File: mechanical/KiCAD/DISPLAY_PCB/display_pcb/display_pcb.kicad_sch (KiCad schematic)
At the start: 52 parts, among them J1 USB_C_Receptacle_USB2.0_16P, J2 Conn_01x18_Socket, J3 Conn_01x01_Pin, J4 Conn_01x01_Pin, J5 Conn_01x02_Pin, Q1 AO3401A, Q2 FS8205, U1 ESP32-S3-WROOM-1, U2 DW01A, U3 USBLC6-2P6, U4 TP4056-42-ESOP8, U5 TLV75733PDBV

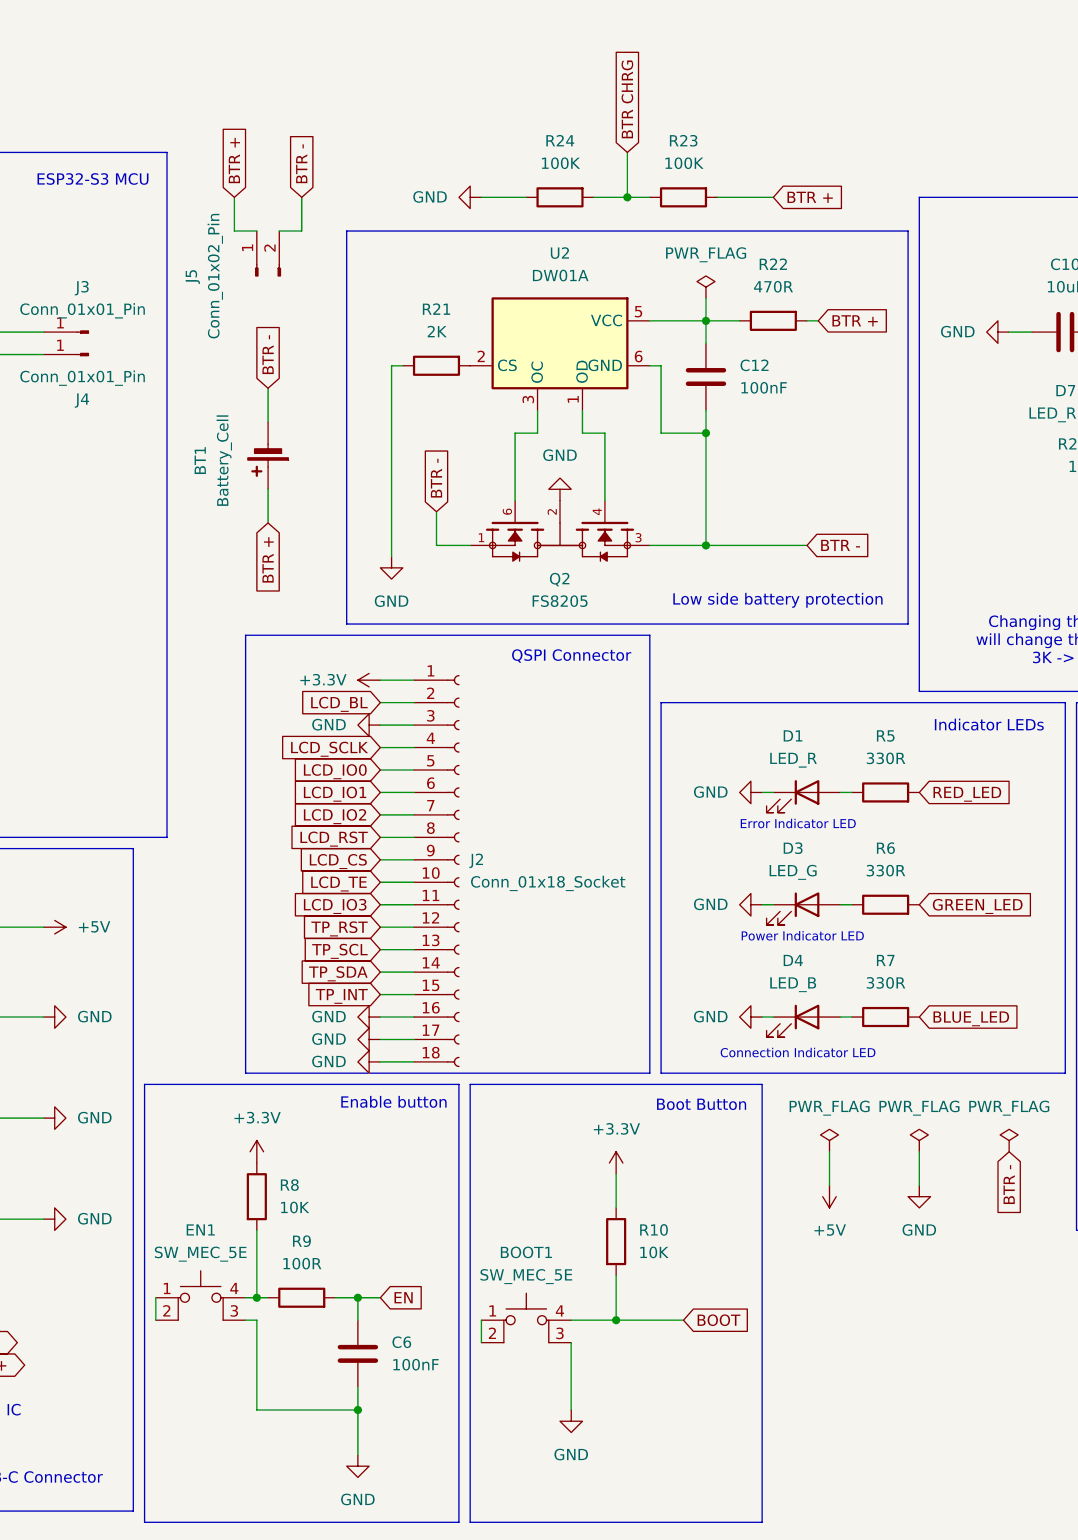
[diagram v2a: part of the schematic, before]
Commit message: Related components are grouped together, they are roughly placed on the PCB. The battery protection may have to go due space limitations (most LiPO batteries has built-in protection). The PCB will be spaced out with extra spacers so the current keepout zones on the front copper face may be used.
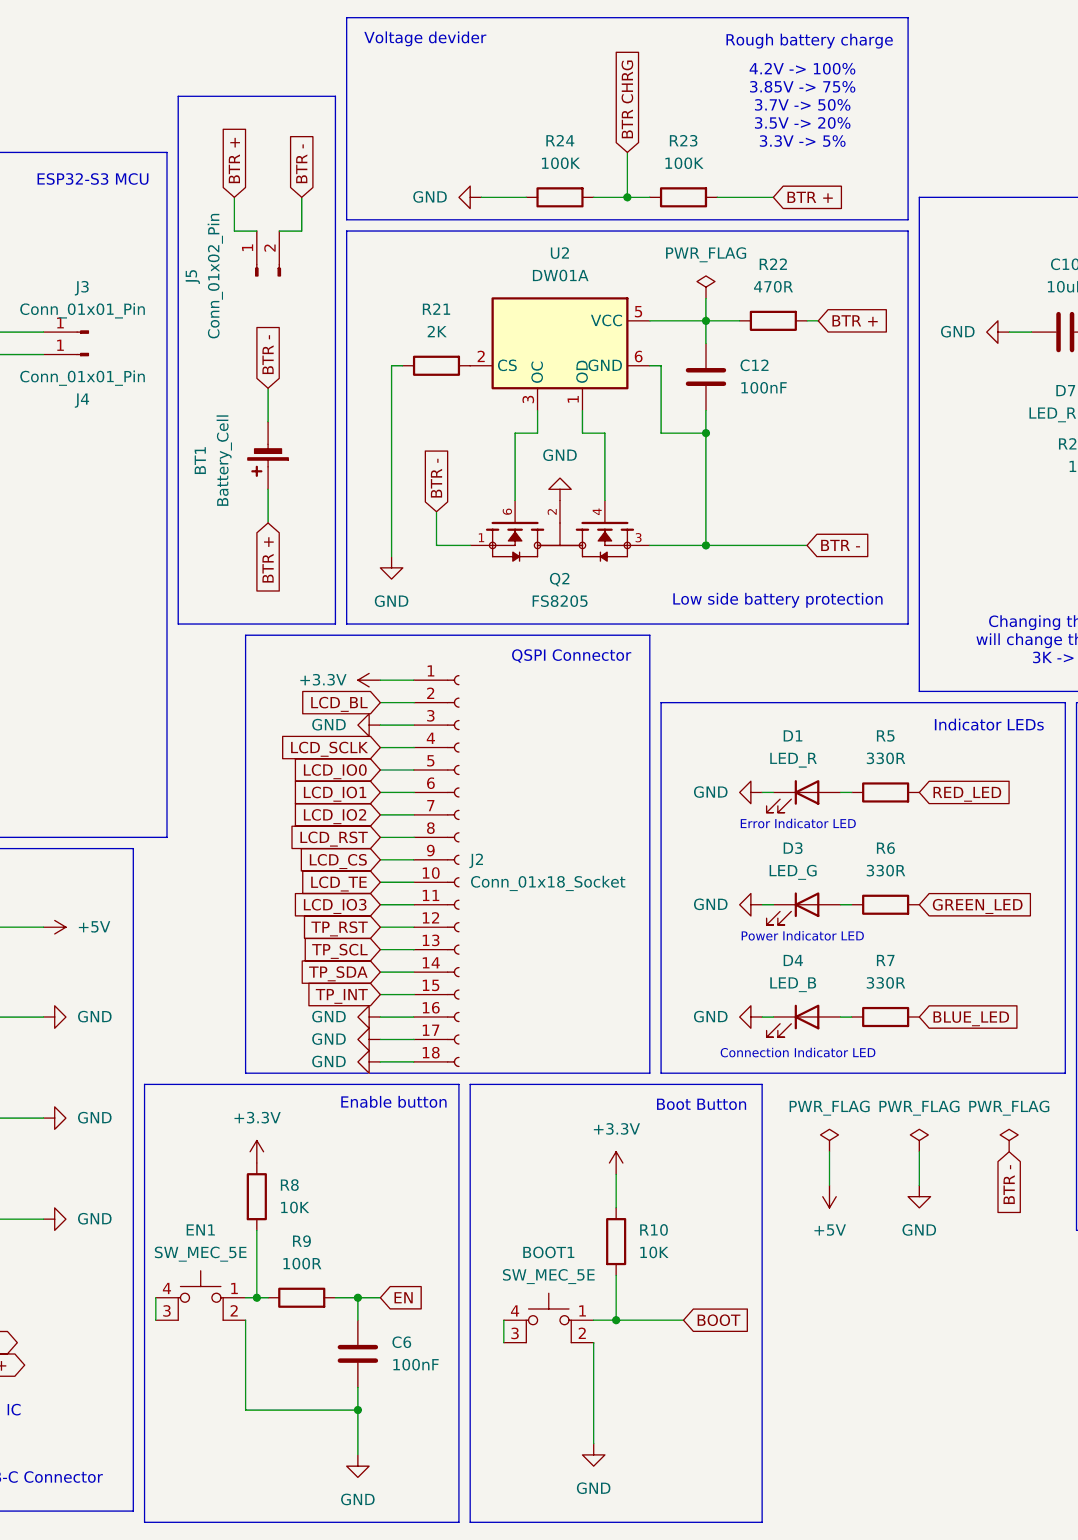
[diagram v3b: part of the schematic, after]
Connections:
- net BOOT: now also BOOT1.1; no longer BOOT1.4 (A)
- net GND: now also BOOT1.2, EN1.2; no longer BOOT1.3 (K), EN1.3 (K)
- net at R8.2, R9.1: now also EN1.1; no longer EN1.4 (A)
- new net: EN1.3 (K), EN1.4 (A)
- new net: BOOT1.3 (K), BOOT1.4 (A)
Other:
- note added: "4.2V -> 100% 3.85V -> 75% 3.7V -> 50% 3.5V -> 20% 3.3V -> 5%"
- note added: "Rough battery charge"
- note added: "Voltage devider"
- moved on the sheet: BOOT1
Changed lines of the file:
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@@
 	)
 	(rectangle
+		(start 129.54 26.67)
+		(end 193.04 49.53)
+		(stroke
+			(width 0)
+			(type default)
+		)
+		(fill
+			(type none)
+		)
+	)
+	(rectangle
 		(start 15.24 41.91)
 		(end 109.22 119.38)
@@
 	)
 	(rectangle
+		(start 110.49 35.56)
+		(end 128.27 95.25)
+		(stroke
+			(width 0)
+			(type default)
+		)
+		(fill
+			(type none)
+		)
+	)
+	(rectangle
 		(start 118.11 96.52)
 		(end 163.83 146.05)
@@
 		)
 	)
+	(text "4.2V -> 100%\n3.85V -> 75%\n3.7V -> 50%\n3.5V -> 20%\n3.3V -> 5%"
+		(exclude_from_sim no)
+		(at 181.102 36.83 0)
+		(effects
+			(font
+				(size 1.27 1.27)
+			)
+		)
+	)
 	(text "Connection Indicator LED"
 		(exclude_from_sim no)
@@
 		)
 	)
+	(text "Rough battery charge"
+		(exclude_from_sim no)
+		(at 181.864 29.464 0)
+		(effects
+			(font
+				(size 1.27 1.27)
+			)
+		)
+	)
 	(text "Changing the R18 resistor value\nwill change the charging amperage\n3K -> 400mA charge"
 		(exclude_from_sim no)
@@
 		)
 	)
+	(text "Voltage devider "
+		(exclude_from_sim no)
+		(at 138.43 29.21 0)
+		(effects
+			(font
+				(size 1.27 1.27)
+			)
+		)
+	)
 	(text "Boot Button"
 		(exclude_from_sim no)
@@
 	)
 	(junction
-		(at 130.81 184.15)
-		(diameter 0)
-		(color 0 0 0 0)
-	)
-	(junction
 		(at 73.66 129.54)
 		(diameter 0)
@@
 	)
 	(junction
-		(at 160.02 173.99)
+		(at 161.29 46.99)
 		(diameter 0)
 		(color 0 0 0 0)
 	)
 	(junction
-		(at 161.29 46.99)
+		(at 215.9 62.23)
 		(diameter 0)
 		(color 0 0 0 0)
 	)
 	(junction
-		(at 215.9 62.23)
+		(at 160.02 173.99)
 		(diameter 0)
 		(color 0 0 0 0)
@@
 	)
 	(junction
+		(at 130.81 184.15)
+		(diameter 0)
+		(color 0 0 0 0)
+	)
+	(junction
 		(at 223.52 139.7)
 		(diameter 0)
@@
 	(wire
 		(pts
-			(xy 119.38 173.99) (xy 118.11 173.99)
-		)
-		(stroke
-			(width 0)
-			(type default)
-		)
-	)
-	(wire
-		(pts
 			(xy 133.35 114.3) (xy 137.16 114.3)
 		)
@@
 	(wire
 		(pts
-			(xy 154.94 173.99) (xy 160.02 173.99)
-		)
-		(stroke
-			(width 0)
-			(type default)
-		)
-	)
-	(wire
-		(pts
 			(xy 194.31 154.94) (xy 194.31 158.75)
 		)
@@
 	(wire
 		(pts
-			(xy 119.38 173.99) (xy 119.38 184.15)
-		)
-		(stroke
-			(width 0)
-			(type default)
-		)
-	)
-	(wire
-		(pts
 			(xy 19.05 173.99) (xy 30.48 173.99)
 		)
@@
 	(wire
 		(pts
+			(xy 157.48 173.99) (xy 160.02 173.99)
+		)
+		(stroke
+			(width 0)
+			(type default)
+		)
+	)
+	(wire
+		(pts
 			(xy 219.71 80.01) (xy 228.6 80.01)
 		)
@@
 	(wire
 		(pts
-			(xy 154.94 176.53) (xy 154.94 184.15)
+			(xy 157.48 176.53) (xy 157.48 187.96)
 		)
 		(stroke
@@
 	(wire
 		(pts
+			(xy 118.11 184.15) (xy 130.81 184.15)
+		)
+		(stroke
+			(width 0)
+			(type default)
+		)
+	)
+	(wire
+		(pts
 			(xy 73.66 139.7) (xy 73.66 162.56)
 		)
@@
 	(wire
 		(pts
+			(xy 147.32 173.99) (xy 147.32 176.53)
+		)
+		(stroke
+			(width 0)
+			(type default)
+		)
+	)
+	(wire
+		(pts
 			(xy 156.21 71.12) (xy 156.21 73.66)
 		)
@@
 	(wire
 		(pts
-			(xy 119.38 184.15) (xy 130.81 184.15)
-		)
-		(stroke
-			(width 0)
-			(type default)
-		)
-	)
-	(wire
-		(pts
 			(xy 68.58 129.54) (xy 73.66 129.54)
 		)
@@
 	(wire
 		(pts
-			(xy 107.95 171.45) (xy 107.95 173.99)
+			(xy 156.21 73.66) (xy 158.75 73.66)
 		)
 		(stroke
@@
 	(wire
 		(pts
-			(xy 156.21 73.66) (xy 158.75 73.66)
+			(xy 161.29 46.99) (xy 163.83 46.99)
 		)
 		(stroke
@@
 	(wire
 		(pts
-			(xy 161.29 46.99) (xy 163.83 46.99)
+			(xy 130.81 181.61) (xy 130.81 184.15)
 		)
 		(stroke
@@
 	(wire
 		(pts
-			(xy 144.78 173.99) (xy 144.78 176.53)
+			(xy 107.95 171.45) (xy 107.95 173.99)
 		)
 		(stroke
@@
 	(wire
 		(pts
+			(xy 130.81 184.15) (xy 130.81 189.23)
+		)
+		(stroke
+			(width 0)
+			(type default)
+		)
+	)
+	(wire
+		(pts
 			(xy 160.02 157.48) (xy 160.02 161.29)
 		)
@@
 	(wire
 		(pts
+			(xy 118.11 173.99) (xy 118.11 184.15)
+		)
+		(stroke
+			(width 0)
+			(type default)
+		)
+	)
+	(wire
+		(pts
 			(xy 241.3 55.88) (xy 241.3 62.23)
 		)
@@
 	(wire
 		(pts
-			(xy 130.81 181.61) (xy 130.81 189.23)
-		)
-		(stroke
-			(width 0)
-			(type default)
-		)
-	)
-	(wire
-		(pts
 			(xy 264.16 71.12) (xy 271.78 71.12)
 		)
@@
 		(lib_id "Switch:SW_MEC_5E")
 		(at 113.03 173.99 0)
+		(mirror y)
 		(unit 1)
 		(body_style 1)
@@
 	(symbol
 		(lib_id "power:GND")
-		(at 154.94 184.15 0)
+		(at 157.48 187.96 0)
 		(unit 1)
 		(body_style 1)
@@
 		(fields_autoplaced yes)
 		(property "Reference" "#PWR018"
-			(at 154.94 190.5 0)
+			(at 157.48 194.31 0)
 			(hide yes)
 			(show_name no)
@@
 		)
 		(property "Value" "GND"
-			(at 154.94 189.23 0)
+			(at 157.48 193.04 0)
 			(show_name no)
 			(do_not_autoplace no)
@@
 		)
 		(property "Footprint" ""
-			(at 154.94 184.15 0)
+			(at 157.48 187.96 0)
 			(hide yes)
 			(show_name no)
@@
 		)
 		(property "Datasheet" ""
-			(at 154.94 184.15 0)
+			(at 157.48 187.96 0)
 			(hide yes)
 			(show_name no)
@@
 		)
 		(property "Description" "Power symbol creates a global label with name \"GND\" , ground"
-			(at 154.94 184.15 0)
+			(at 157.48 187.96 0)
 			(hide yes)
 			(show_name no)
@@
 	(symbol
 		(lib_id "Switch:SW_MEC_5E")
-		(at 149.86 176.53 0)
+		(at 152.4 176.53 0)
+		(mirror y)
 		(unit 1)
 		(body_style 1)
@@
 		(fields_autoplaced yes)
 		(property "Reference" "BOOT1"
-			(at 149.86 166.37 0)
+			(at 152.4 166.37 0)
 			(show_name no)
 			(do_not_autoplace no)
@@
 		)
 		(property "Value" "SW_MEC_5E"
-			(at 149.86 168.91 0)
+			(at 152.4 168.91 0)
 			(show_name no)
 			(do_not_autoplace no)
@@
 		)
 		(property "Footprint" "Button_Switch_SMD:SW_SPST_EVQP2_MiddlePushTravel_H2.5mm"
-			(at 149.86 168.91 0)
+			(at 152.4 168.91 0)
 			(hide yes)
 			(show_name no)
@@
 		)
 		(property "Datasheet" "https://www.apem.com/medias/download/MEC_switches_serie_MULTIMEC5E.pdf"
-			(at 149.86 168.91 0)
+			(at 152.4 168.91 0)
 			(hide yes)
 			(show_name no)
@@
 		)
 		(property "Description" "MEC 5E single pole normally-open tactile switch"
-			(at 149.86 176.53 0)
+			(at 152.4 176.53 0)
 			(hide yes)
 			(show_name no)

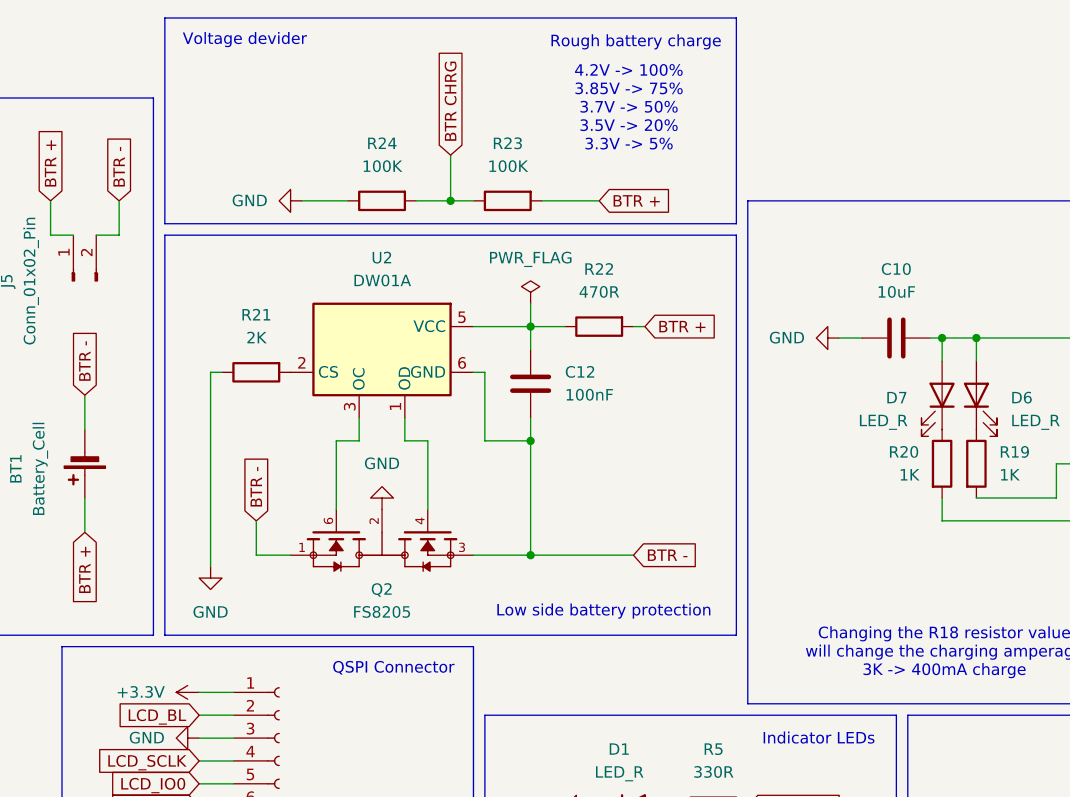
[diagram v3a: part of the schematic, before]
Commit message: The components are placed, the flex cable connector pinout has to be changed, the protection circuit was deleted because of limited space.
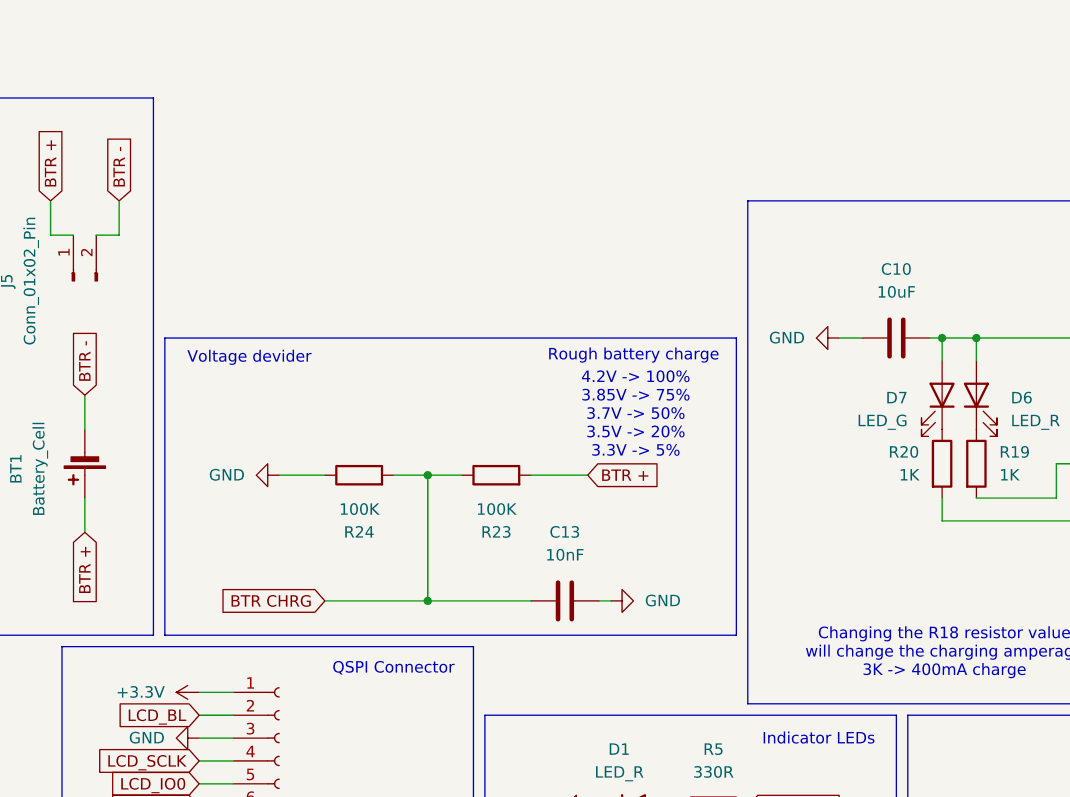
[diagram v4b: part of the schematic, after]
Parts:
- removed C12: 100nF, Capacitor_SMD:C_0805_2012Metric, symbol Device:C
- removed Q2: FS8205, Package_SO:TSSOP-8_4.4x3mm_P0.65mm, symbol FS8205:FS8205
- removed R21: 2K, Resistor_SMD:R_0805_2012Metric, symbol Device:R
- removed R22: 470R, Resistor_SMD:R_0805_2012Metric, symbol Device:R
- removed U2: DW01A, Package_TO_SOT_SMD:SOT-23-6, symbol Battery_Management:DW01A
- added C13: 10nF, Capacitor_SMD:C_0805_2012Metric, symbol Device:C
- D7: value LED_R -> LED_G
- J5: footprint Connector_JST:JST_PH_S2B-PH-K_1x02_P2.00mm_Horizontal -> Connector_Molex:Molex_PicoBlade_53261-0271_1x02-1MP_P1.25mm_Horizontal
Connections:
- net BTR CHRG: now also C13.1
- net GND: now also C13.2
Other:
- note removed: "Low side battery protection"
- moved on the sheet: R23, R24

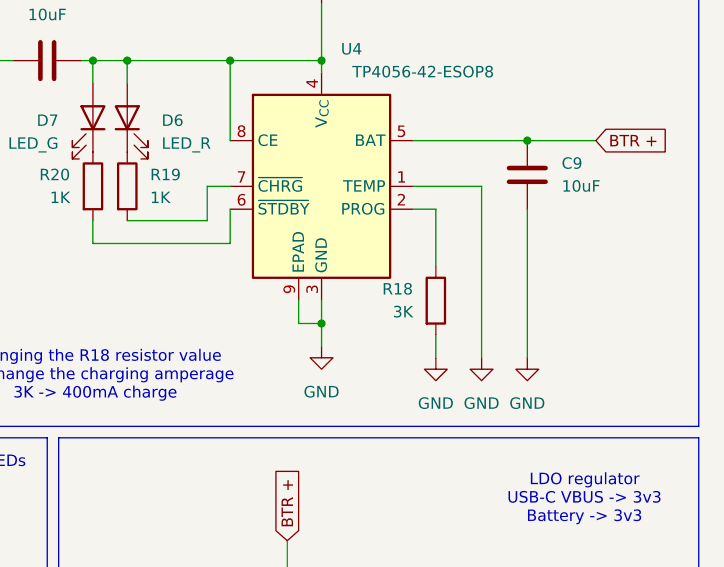
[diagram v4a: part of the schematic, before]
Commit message: Relocated some components for the high signal routes, the flex cable connector is still not in a fixed location. The buttons and the LEDs may have to be relocated for easier routing.
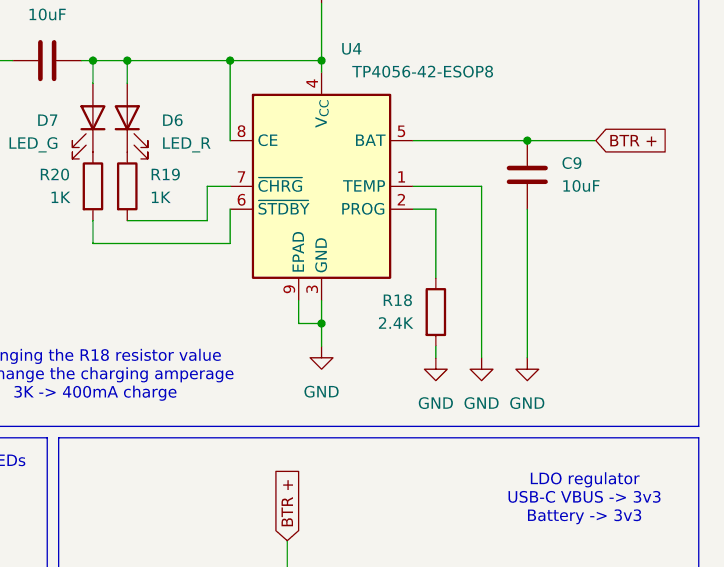
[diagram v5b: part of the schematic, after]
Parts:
- R18: value 3K -> 2.4K
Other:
- moved on the sheet: R18
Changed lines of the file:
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@@
 	(wire
 		(pts
-			(xy 254 92.71) (xy 254 95.25)
+			(xy 254 93.98) (xy 254 95.25)
 		)
 		(stroke
@@
 	(wire
 		(pts
-			(xy 254 78.74) (xy 254 85.09)
+			(xy 254 78.74) (xy 254 86.36)
 		)
 		(stroke
@@
 	(symbol
 		(lib_id "Device:R")
-		(at 254 88.9 0)
+		(at 254 90.17 0)
 		(unit 1)
 		(body_style 1)
@@
 		(fields_autoplaced yes)
 		(property "Reference" "R18"
-			(at 251.46 87.6299 0)
+			(at 251.46 88.8999 0)
 			(show_name no)
 			(do_not_autoplace no)
@@
 			)
 		)
-		(property "Value" "3K"
-			(at 251.46 90.1699 0)
+		(property "Value" "2.4K"
+			(at 251.46 91.4399 0)
 			(show_name no)
 			(do_not_autoplace no)
@@
 		)
 		(property "Footprint" "Resistor_SMD:R_0805_2012Metric"
-			(at 252.222 88.9 90)
+			(at 252.222 90.17 90)
 			(hide yes)
 			(show_name no)
@@
 		)
 		(property "Datasheet" ""
-			(at 254 88.9 0)
+			(at 254 90.17 0)
 			(hide yes)
 			(show_name no)
@@
 		)
 		(property "Description" "Resistor"
-			(at 254 88.9 0)
+			(at 254 90.17 0)
 			(hide yes)
 			(show_name no)
